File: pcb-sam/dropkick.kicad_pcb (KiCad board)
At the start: 2 copper layers, 44.5 x 50.8 mm, 48 parts, among them J1 Conn_01x08, SW1 450405020524, SW2 KMR211NG_LFS, U1 SPX3819-3.3, U2 SAM-M8Q-0-10, U3 MCP73831T-2ACI/OT, U4 ATSAMD21G18A-AUT, U5 DPS310XTSA1, U6 MPU-6050, X1 microUSB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

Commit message: v3 SAM PCB
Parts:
- removed X1: microUSB, lib_fr:4UCONN_20329_V2
- added C13: 10nF, Capacitor_SMD:C_0402_1005Metric, F.Cu at (103.1, 70.2)
- added J2: USB C USB2.0, Connector_USB:USB_C_Receptacle_GCT_USB4085, F.Cu at (93.2, 50.4)
- added R11: 5.1K, Resistor_SMD:R_0402_1005Metric, F.Cu at (88.9, 53.3)
- added R12: 5.1K, Resistor_SMD:R_0402_1005Metric, F.Cu at (87.5, 53.3)
- C10: footprint Capacitor_SMD:C_0603_1608Metric -> Capacitor_SMD:C_0402_1005Metric
- C11, C12: footprint lib_fr:0603-NO -> Capacitor_SMD:C_0402_1005Metric
- C3, C4, C8: value 10µF -> 10uF
- CHG1: value ORANGE -> LTST-C191KFKT
- D2, L1: value GREEN -> LTST-S270KGKT
- L2: value RED -> LTST-S270KRKT
- R1, R2: value 100k -> 100K
- U4: value ATSAMD21G18A-AUT -> ATSAMD21G18A-AUT
- X3: value microsd -> MEM2061-01-188-00-A
- moved C11 4.79 mm to (103.1, 68.0), turned to 90 degrees
- moved R2 4.15 mm to (92.5, 54.0), turned to 90 degrees
- moved C12 1.68 mm to (97.6, 65.8), turned to 90 degrees
- moved SW2 1.55 mm to (100.1, 50.6), turned to 180 degrees
- moved U1 1.43 mm to (95.2, 54.6)
- moved C4 1.00 mm to (97.7, 54.9), turned to 90 degrees
- moved C2 0.91 mm to (85.6, 54.8)
- moved U6 0.90 mm to (99.9, 68.9)
- moved C9 0.80 mm to (89.1, 58.7)
- moved U4 0.80 mm to (89.3, 65.3)
- moved X4 0.80 mm to (82.9, 61.6)
- moved C1 0.80 mm to (82.0, 64.8)
- moved C6 0.80 mm to (80.1, 60.8)
- moved C7 0.80 mm to (80.1, 62.4)
- moved R1 0.80 mm to (81.8, 69.3)
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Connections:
- U6 pad 12: /INT -> /D11
- U6 pad 8: +3V3 -> Net-(C13-Pad2)
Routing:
- net +3V3: track 205.2 -> 175.3 mm, vias 7 -> 2
- net /D13: track 22.9 -> 47.7 mm, vias 0 -> 2
- net /REGOUT: track 24.1 -> 1.26 mm, vias 4 -> 0
- net /D-: track 17.9 -> 39.2 mm
- net /D+: track 17.1 -> 37.0 mm, vias 0 -> 2
- net GND: track 104.5 -> 122.2 mm, vias 19 -> 17
- net Net-(J2-PadB5): track 0.00 -> 10.0 mm
- net /D11: track 0.00 -> 9.82 mm, vias 0 -> 2
- net /SCK: track 24.0 -> 31.8 mm
- net /MOSI: track 28.1 -> 21.9 mm
- net /SCL: track 47.4 -> 41.8 mm, vias 2 -> 4
- net /D7: track 22.4 -> 17.6 mm
- net Net-(J2-PadA5): track 0.00 -> 4.46 mm, vias 0 -> 1
- net /SDA: track 57.7 -> 54.2 mm, vias 3 -> 0
- net /VBACKUP: track 29.2 -> 26.8 mm, vias 2 -> 0
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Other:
- board text added: "Dropkick V3-SAM Copyright (c) 2023 Riley Rainey https://GitHub.com/rrainey/dropkick/"
- board text added: "Dropkick V3-SAM Riley Rainey"
- board text removed: "Dropkick V2-SAM Copyright (c) 2022 Riley Rainey https://GitHub.com/rrainey/dropkick/"
- board text removed: "Dropkick V2-SAM Riley Rainey"

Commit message: V4 SAM PCB
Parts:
- removed D2: LTST-S270KGKT, lib_fr:CHIPLED_0603_NOOUTLINE
- removed H4: MountingHole, lib_fr:MOUNTINGHOLE_2.5_PLATED
- removed JP1: 3221-10-0300-00-TR, lib_fr:3221-10-0300-00-TR
- removed X3: MEM2061-01-188-00-A, lib_fr:MICROSD
- removed X4: 32768Hz, lib_fr:XTAL3215
- added C14: 10nF, Capacitor_SMD:C_0603_1608Metric, F.Cu at (101.3, 59.1)
- added J3: Conn_01x08, Connector_PinHeader_2.54mm:PinHeader_1x09_P2.54mm_Vertical, F.Cu at (106.0, 54.9)
- added J4: 3221-10-0300-00-TR, lib_fr:3221-10-0300-00-TR, B.Cu at (97.6, 55.7)
- added L3: LTST-S270KGKT, lib_fr:CHIPLED_0603_NOOUTLINE, F.Cu at (75.0, 46.7)
- added X1: MEM2061-01-188-00-A, lib_fr:MICROSD, B.Cu at (79.7, 75.7)
- C10: footprint Capacitor_SMD:C_0402_1005Metric -> Capacitor_SMD:C_0603_1608Metric
- C11: value 0.1uF -> 2.2uF; footprint Capacitor_SMD:C_0402_1005Metric -> Capacitor_SMD:C_0603_1608Metric
- C12: value 2.2nF -> 100nF; footprint Capacitor_SMD:C_0402_1005Metric -> Capacitor_SMD:C_0603_1608Metric
- C13: value 10nF -> 100nF; footprint Capacitor_SMD:C_0402_1005Metric -> Capacitor_SMD:C_0603_1608Metric
- D1: value MBR120 -> SCHOTTKY 20V; footprint lib_fr:SOD-123 -> Diode_SMD:D_SOD-123F
- J1: value Conn_01x08 -> USB C USB2.0; footprint Connector_PinHeader_2.54mm:PinHeader_1x09_P2.54mm_Vertical -> Connector_USB:USB_C_Receptacle_GCT_USB4085
- J2: value USB C USB2.0 -> BATT; footprint Connector_USB:USB_C_Receptacle_GCT_USB4085 -> lib_fr:JSTPH2; moved to B.Cu
- R1, R2: value 100K -> 5.1K; footprint lib_fr:0603-NO -> Resistor_SMD:R_0402_1005Metric
- R10, R8, R9: value 10K -> 2.2K
- R11, R12: value 5.1K -> 10K; footprint Resistor_SMD:R_0402_1005Metric -> Resistor_SMD:R_0603_1608Metric
- R3: footprint lib_fr:0603-NO -> Resistor_SMD:R_0603_1608Metric
- R4: value 10K -> 100K
- R5: value 1K -> 100K
- R6: value 2.2K -> 10K
- U2: value SAM-M8Q-0-10 -> SAM-M10Q
- U5: value DPS310XTSA1 -> BMP390; footprint lib_fr:DPS310XTSA1 -> lib_fr:LGA10_BMP390_BOS
- U6: value MPU-6050 -> ICM-42688-P; footprint lib_fr:QFN24_4MM_SMSC -> lib_fr:PQFN50P300X250X97-14N
- X2: value JSTPH -> 32768Hz; footprint lib_fr:JSTPH2 -> lib_fr:XTAL3215; moved to F.Cu
- moved R10 32.0 mm to (73.4, 48.3), turned to 90 degrees
- moved R9 22.2 mm to (82.2, 51.1), turned to 90 degrees
- moved J2 22.0 mm to (71.9, 56.2), turned to 90 degrees
- moved R5 20.5 mm to (83.4, 69.4), turned to 90 degrees
- moved R6 20.0 mm to (79.7, 54.1), turned to -90 degrees
- moved R1 19.0 mm to (91.4, 52.9), turned to -90 degrees
- moved R12 19.0 mm to (103.7, 63.2), turned to 90 degrees
- moved C3 17.8 mm to (97.8, 54.3), turned to -90 degrees
- moved R11 16.0 mm to (103.7, 59.5)
- moved R4 14.7 mm to (92.6, 53.2), turned to -90 degrees
- moved J1 13.3 mm to (93.2, 50.4), turned to 180 degrees
- moved L2 12.5 mm to (84.1, 46.4), turned to 0 degrees
- moved X2 12.2 mm to (82.8, 61.7)
- moved R8 12.0 mm to (84.1, 51.1), turned to 90 degrees
- moved C11 11.2 mm to (95.5, 59.8)
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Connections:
- C11 pad 1: /REGOUT -> +3V3
- C12 pad 1: /CPOUT -> +3V3
- C13 pad 2: Net-(C13-Pad2) -> GND
- L1 pad A: /D8 -> Net-(L1-PadA)
- L1 pad C: Net-(L1-PadC) -> GND
- R1 pad 1: VBAT -> Net-(J1-PadA5)
- R1 pad 2: /D9 -> GND
- R10 pad 2: /SDA -> Net-(L3-PadA)
- R11 pad 1: Net-(J2-PadA5) -> +3V3
- R11 pad 2: GND -> /SCL
- R12 pad 1: Net-(J2-PadB5) -> +3V3
- R12 pad 2: GND -> /SDA
- R2 pad 1: VBUS -> Net-(J1-PadB5)
- R2 pad 2: /EN -> GND
- R3 pad 1: /D9 -> VBAT
- R3 pad 2: GND -> /D9
- R4 pad 1: Net-(R4-Pad1) -> VBUS
- R4 pad 2: GND -> /EN
- R5 pad 1: Net-(CHG1-PadC) -> /D9
- R5 pad 2: Net-(R5-Pad2) -> GND
- R6 pad 1: /D13 -> Net-(R6-Pad1)
- R6 pad 2: Net-(L2-PadA) -> GND
- R7 pad 1: Net-(L1-PadC) -> Net-(CHG1-PadC)
- R7 pad 2: GND -> Net-(R7-Pad2)
- R8 pad 1: +3V3 -> /D13
- R8 pad 2: Net-(D2-PadA) -> Net-(L2-PadA)
- R9 pad 1: +3V3 -> /D8
- R9 pad 2: /SCL -> Net-(L1-PadA)
- SW1 pad 2: Net-(SW1-Pad2) -> Net-(J2-Pad2)
- U3 pad 1: Net-(R5-Pad2) -> Net-(R7-Pad2)
- U3 pad 5: Net-(R4-Pad1) -> Net-(R6-Pad1)
- U5 pad 1: GND -> +3V3
- U5 pad 2: GND -> /SCL
- U5 pad 3: /SDA -> GND
- U5 pad 4: /SCL -> /SDA
- U5 pad 7: GND -> /D6
- U5 pad 8: +3V3 -> GND
- U6 pad 10: /REGOUT -> unconnected-(U6-Pad10)
- U6 pad 12: /D11 -> +3V3
- U6 pad 13: +3V3 -> /SCL
- U6 pad 14: (no net) -> /SDA
- U6 pad 2: (no net) -> unconnected-(U6-Pad2)
- U6 pad 3: (no net) -> unconnected-(U6-Pad3)
- U6 pad 4: (no net) -> /D11
- U6 pad 5: (no net) -> +3V3
- U6 pad 6: /SDA_EXT -> GND
- U6 pad 7: /SCL_EXT -> GND
- U6 pad 8: Net-(C13-Pad2) -> +3V3
- U6 pad 9: /AD0 -> /D12
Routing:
- net GND: track 122.2 -> 88.7 mm, vias 17 -> 25
- net /D13: track 47.7 -> 21.1 mm, vias 2 -> 0
- net /D-: track 39.2 -> 18.1 mm, vias 0 -> 2
- net /D+: track 37.0 -> 17.3 mm
- net /D6: track 0.00 -> 12.4 mm, vias 0 -> 2
- net Net-(J2-PadB5): track 10.0 -> 0.00 mm
- net Net-(J2-Pad2): track 0.00 -> 9.65 mm
- net Net-(SW1-Pad2): track 9.58 -> 0.00 mm
- net /D12: track 0.00 -> 9.51 mm, vias 0 -> 2
- net Net-(J1-PadB5): track 0.00 -> 8.06 mm
- net /SDA: track 54.2 -> 47.1 mm, vias 0 -> 2
- net /D7: track 17.6 -> 24.6 mm, vias 1 -> 3
- net /D8: track 27.8 -> 21.4 mm
- net /AREF: track 26.4 -> 32.3 mm
- net /D11: track 9.82 -> 15.6 mm
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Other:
- board text added: "Dropkick V4-SAM Copyright (c) 2023 Riley Rainey https://GitHub.com/rrainey/dropkick/"
- board text added: "Dropkick V4-SAM Riley Rainey"
- board text removed: "Dropkick V3-SAM Copyright (c) 2023 Riley Rainey https://GitHub.com/rrainey/dropkick/"
- board text removed: "Dropkick V3-SAM Riley Rainey"

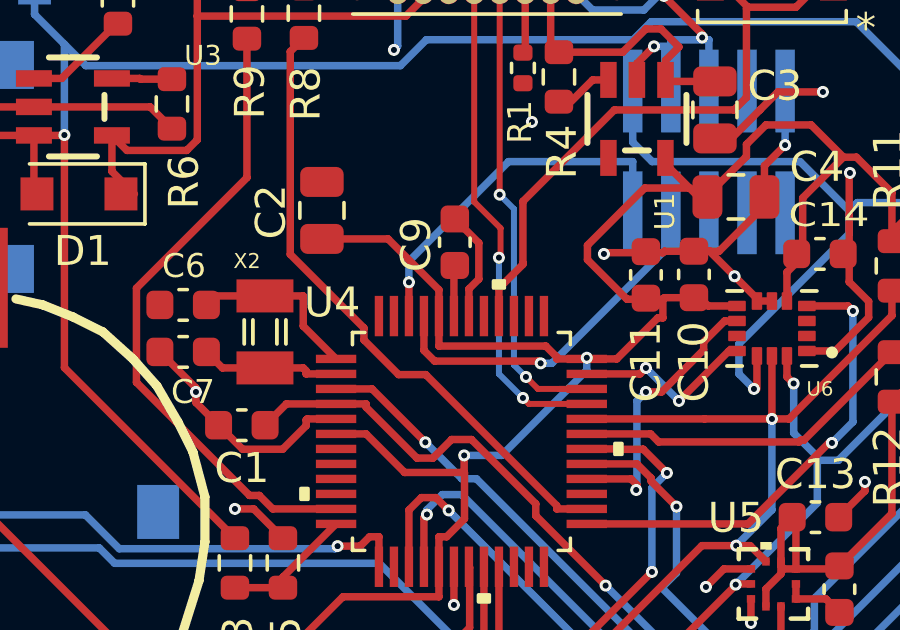
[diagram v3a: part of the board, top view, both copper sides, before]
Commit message: Update paste margins on ICM42688; minor pcb trace
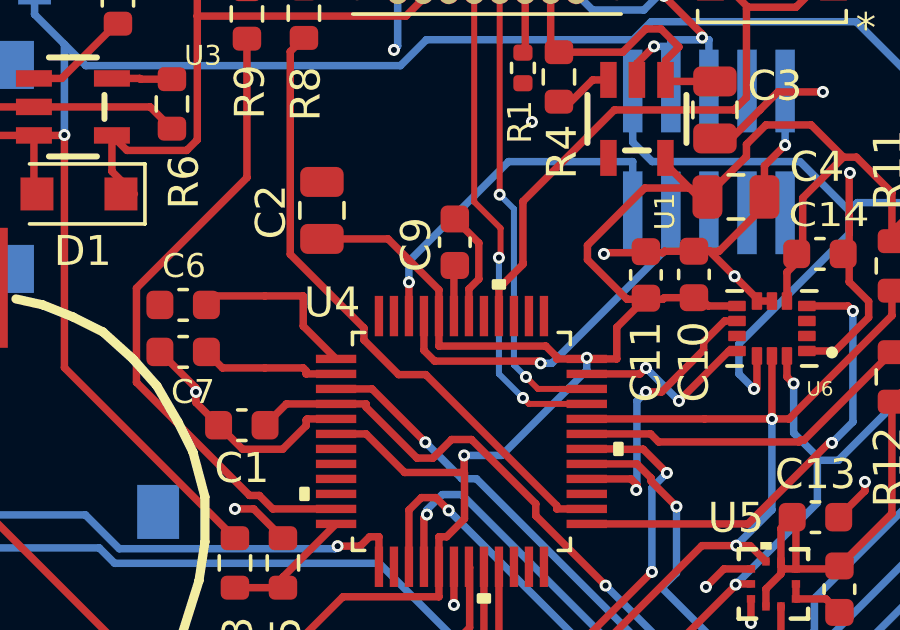
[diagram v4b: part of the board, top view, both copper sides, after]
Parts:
- removed X2: 32768Hz, lib_fr:XTAL3215
